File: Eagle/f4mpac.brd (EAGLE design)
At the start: 59.7 x 81.3 mm, 47 parts, among them CN1 DIP40 MB CONN, IC1 YM2413, IC10 27C128L, IC2 74LS30D, IC3 74LS04D, IC4 LM4558N, IC5 Z80, IC6 74LS30D, IC7 74LS02D, IC8 74LS74D, IC9 74LS125D

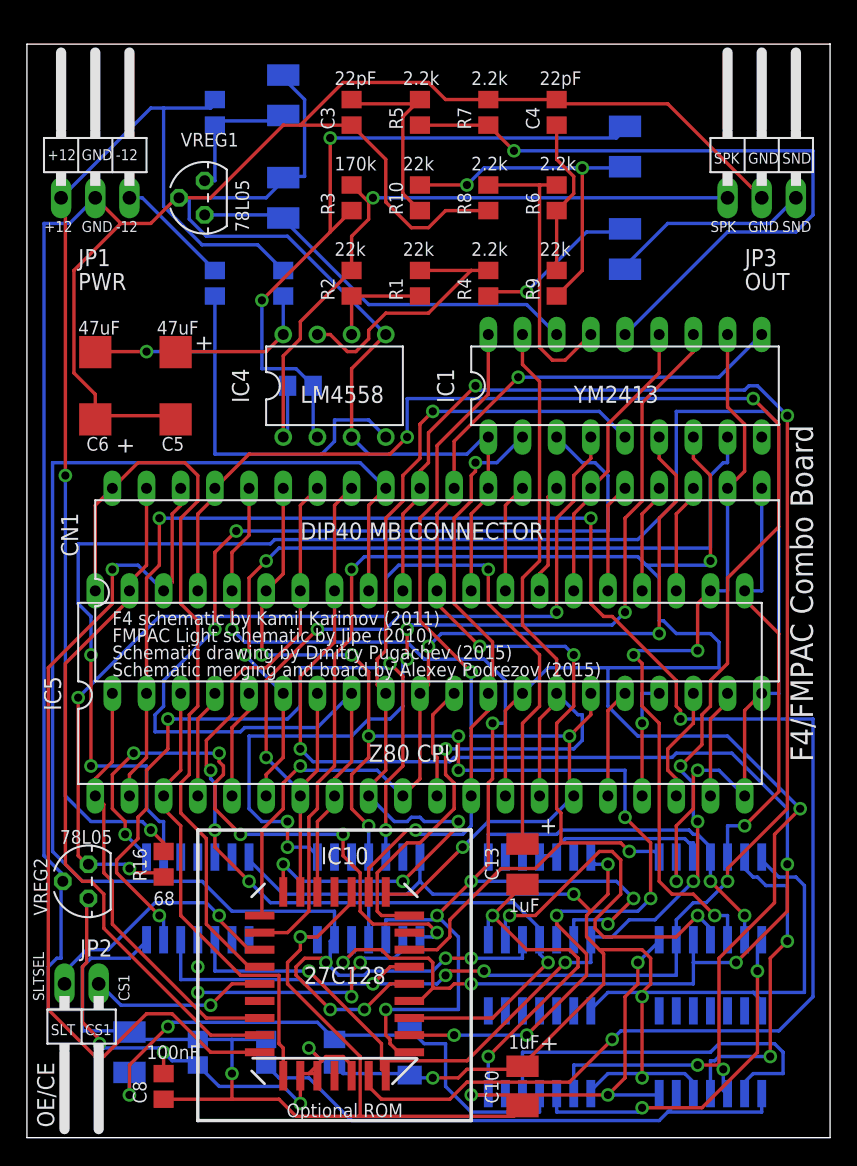
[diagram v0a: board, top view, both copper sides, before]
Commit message: New board version 1.3
New board version 1.3, new combined and selectable ROM, easier to get
ROM chip, corrected names error, blocking capacitors, additional noise
suppressing capacitor
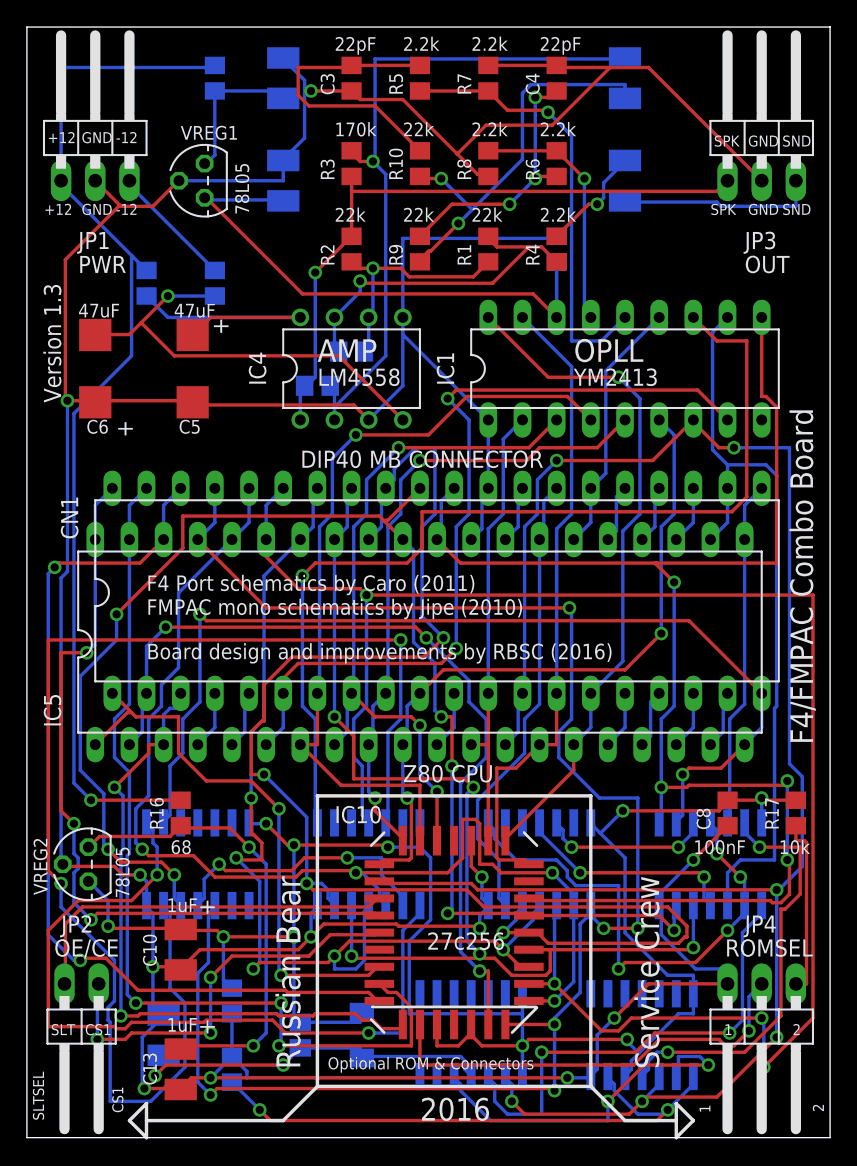
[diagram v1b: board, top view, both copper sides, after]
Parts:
- added C15: 100nF, rcl:C0805
- added C16: 1nF, rcl:C0805
- added JP4: ROM, pinhead:1X03/90
- added R17: 10k, rcl:R0805
- IC10: value 27C128L -> 27C256L
- moved C8 46.6 mm to (52.1, 24.1)
- moved C13 29.6 mm to (11.4, 5.08)
- moved C10 27.4 mm to (11.4, 14.0)
- moved R9 10.5 mm to (29.2, 66.0)
- moved R12 10.2 mm to (8.89, 63.5)
- moved IC10 9.67 mm to (31.8, 15.2)
- moved R1 5.68 mm to (34.3, 66.0)
- moved R4 5.68 mm to (39.4, 66.0), turned to 90 degrees
- moved IC8 5.24 mm to (33.0, 7.62)
- moved IC9 5.24 mm to (45.7, 7.62)
- moved C1 5.08 mm to (44.5, 71.1)
- moved C2 5.08 mm to (44.5, 78.7)
- moved C11 4.58 mm to (15.2, 10.2), turned to 270 degrees
- moved R16 4.02 mm to (11.4, 24.1)
- moved IC5 3.81 mm to (29.2, 36.8)
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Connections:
- removed net N$10: IC4.7, R1.2, R4.1
- removed net N$29: IC6.6, IC7.4
- new net N$24: IC6.11, IC7.4
- new net N$25: IC10.31, JP4.2
- new net N$26: JP4.1, R17.2
- new net N$27: C16.2, IC4.7, R1.2, R4.1
- net +5VREG: now also R17.1; no longer IC10.31
- net GND: now also C15.1, JP4.3
- net M1: now also IC6.6
- net N$23: now also C15.2
- net N$30: no longer IC6.11
- net N$9: now also C16.1
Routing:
- net A12: track 139.5 -> 62.1 mm, vias 4 -> 3
- net IORQ: track 133.4 -> 74.5 mm, vias 4 -> 2
- net N$22: track 77.8 -> 34.6 mm, vias 3 -> 2
- net N$15: track 54.8 -> 96.1 mm, vias 4 -> 2
- net D3: track 85.8 -> 51.8 mm, vias 2 -> 3
- net N$25: track 0.00 -> 32.8 mm, vias 0 -> 1
- net A5: track 97.9 -> 130.6 mm, vias 11 -> 4
- net A3: track 111.9 -> 81.4 mm
- net N$29: track 29.2 -> 0.00 mm, vias 2 -> 0
- net GND: track 373.0 -> 344.4 mm, vias 7 -> 12
- net M1: track 8.15 -> 34.3 mm
- net N$27: track 0.00 -> 25.9 mm, vias 0 -> 1
- net A1: track 131.1 -> 106.8 mm, vias 6 -> 7
- net D5: track 71.5 -> 47.4 mm, vias 4 -> 2
- net D0: track 69.6 -> 48.1 mm, vias 1 -> 0
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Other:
- board size 59.7 x 81.3 mm -> 59.7 x 82.5 mm
- board text added: "1"
- board text added: "10k"
- board text added: "2"
- board text added: "2016"
- board text added: "27c256"
- board text added: "AMP"
- board text added: "Board design and improvements by RBSC (2016)"
- board text added: "C15"
- board text added: "C16"
- board text added: "F4 Port schematics by Caro (2011)"
- board text added: "FMPAC mono schematics by Jipe (2010)"
- board text added: "JP4"
- board text added: "OPLL"
- board text added: "Optional MSX2+ F4 Port"
- board text added: "Optional ROM & Connectors"
- board text added: "R17"
- board text added: "ROMSEL"
- board text added: "Russian Bear"
- board text added: "Russian Bear Service Crew (C) 2016"
- board text added: "Service Crew"
- board text added: "Version 1.3"
- board text removed: "27C128"
- board text removed: "F4 Register"
- board text removed: "F4 schematic by Kamil Karimov (2011)"
- board text removed: "FMPAC Light schematic by Jipe (2010)"
- board text removed: "MSX2+ F4 Register"
- board text removed: "Optional"
- board text removed: "Optional ROM"
- board text removed: "Schematic drawing by Dmitry Pugachev (2015)"
- board text removed: "Schematic merging and board by Alexey Podrezov (2015)"
- board text removed: "Version 1.2"

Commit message: Updated source and gerber files, added schematics
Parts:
- added SJ1, SJ2: (no value), jumper:SJ_2
- IC10: value 27C256L -> 27C512AL
- JP4: value ROM -> ROMSEL; device pinhead:1X03/90 -> pinhead:1X02/90
- moved R17 19.3 mm to (49.5, 6.35)
- moved C15 8.98 mm to (38.1, 57.1), turned to 180 degrees
- moved C8 3.81 mm to (55.9, 24.1)
- moved C1 1.27 mm to (44.5, 69.8)
- moved C12 1.27 mm to (19.1, 69.8)
- moved IC10 1.27 mm to (30.5, 15.2)
- moved C2 1.27 mm to (44.5, 77.5)
- moved C7 1.27 mm to (19.1, 77.5)
- moved JP4 1.02 mm to (55.6, 7.62)
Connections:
- new net N$10: IC10.31, SJ1.2
- net +5VREG: now also SJ2.1; no longer IC10.2
- net A14: now also SJ1.3
- net A15: now also SJ2.3
- net GND: now also JP4.1; no longer JP4.3
- net N$25: now also IC10.2, SJ2.2; no longer IC10.31, JP4.2
- net N$26: now also JP4.2, SJ1.1; no longer JP4.1
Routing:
- net A14: track 4.34 -> 74.8 mm, vias 0 -> 2
- net N$25: track 32.8 -> 93.6 mm, vias 1 -> 6
- net N$10: track 0.00 -> 57.2 mm, vias 0 -> 4
- net A2: track 107.5 -> 58.6 mm
- net A5: track 130.6 -> 82.8 mm, vias 4 -> 8
- net N$17: track 20.6 -> 68.2 mm, vias 2 -> 4
- net A15: track 4.34 -> 45.6 mm
- net N$15: track 96.1 -> 59.4 mm
- net A1: track 106.8 -> 141.0 mm, vias 7 -> 4
- net A3: track 81.4 -> 113.9 mm, vias 5 -> 7
- net RST: track 19.1 -> 51.1 mm
- net N$18: track 58.2 -> 26.3 mm, vias 2 -> 4
- net A7: track 126.4 -> 95.3 mm
- net N$24: track 16.6 -> 47.6 mm, vias 2 -> 4
- net GND: track 344.4 -> 370.6 mm
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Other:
- board text added: "(C) 2016"
- board text added: "27c128"
- board text added: "27c512"
- board text added: "3"
- board text added: "And Connectors"
- board text added: "CE"
- board text added: "CE/OE"
- board text added: "CS1/RD"
- board text added: "EPROM"
- board text added: "For 27c512 connect OE to RD"
- board text added: "OE"
- board text added: "Optional"
- board text added: "Optional ROM"
- board text added: "RBSC"
- board text added: "ROM"
- board text added: "SJ1"
- board text added: "SJ1 & SJ2: 1-2 for 27c128, 27c256"
- board text added: "SJ1 & SJ2: 2-3 for 27c512"
- board text added: "SJ2"
- board text added: "Selection"
- board text removed: "2016"
- board text removed: "CS1"
- board text removed: "OE/CE"
- board text removed: "Optional ROM & Connectors"
- board text removed: "Russian Bear Service Crew (C) 2016"
- board text removed: "SLT"
